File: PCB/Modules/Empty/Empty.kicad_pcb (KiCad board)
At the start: 2 copper layers, 29 x 59 mm, 4 parts, among them J1 In, J2 In, U1 SP720ABTG

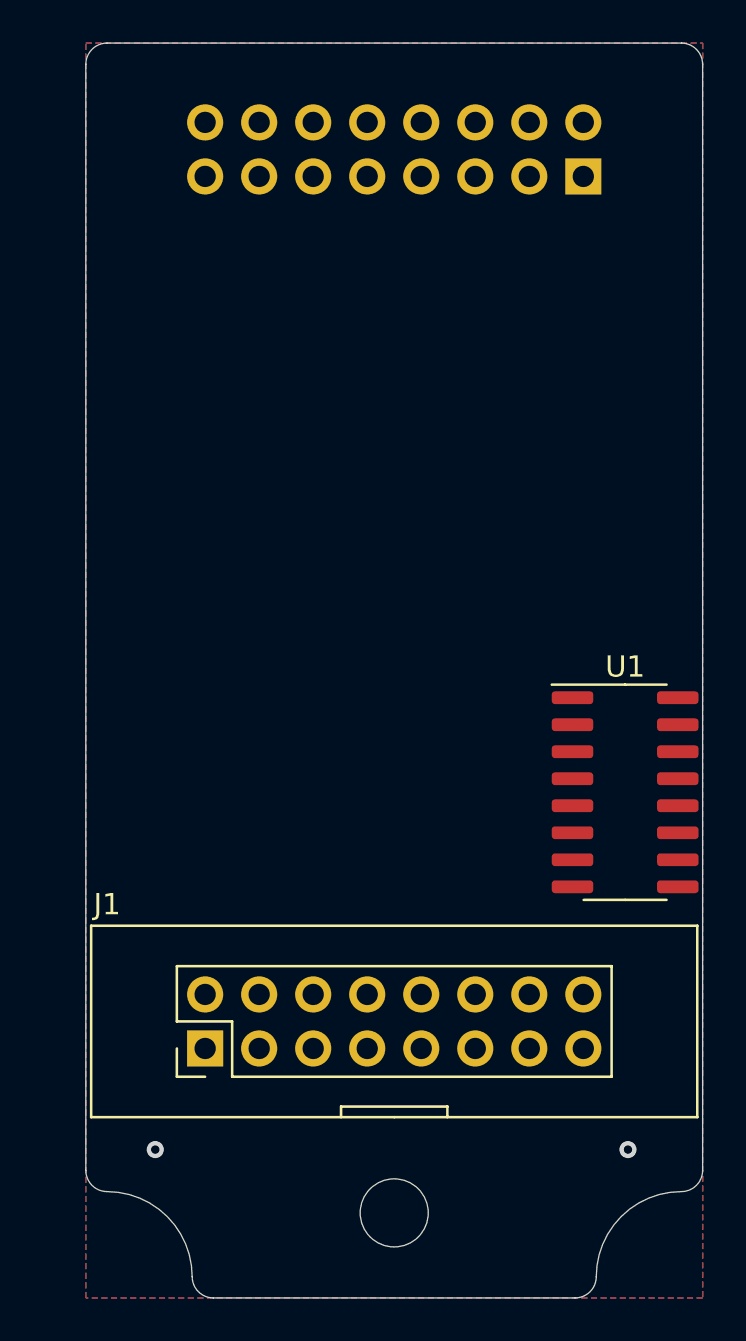
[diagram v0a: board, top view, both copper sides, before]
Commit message: Convert all KiCad to 6.0, clean up libraries, remove files that shouldn't be committed.
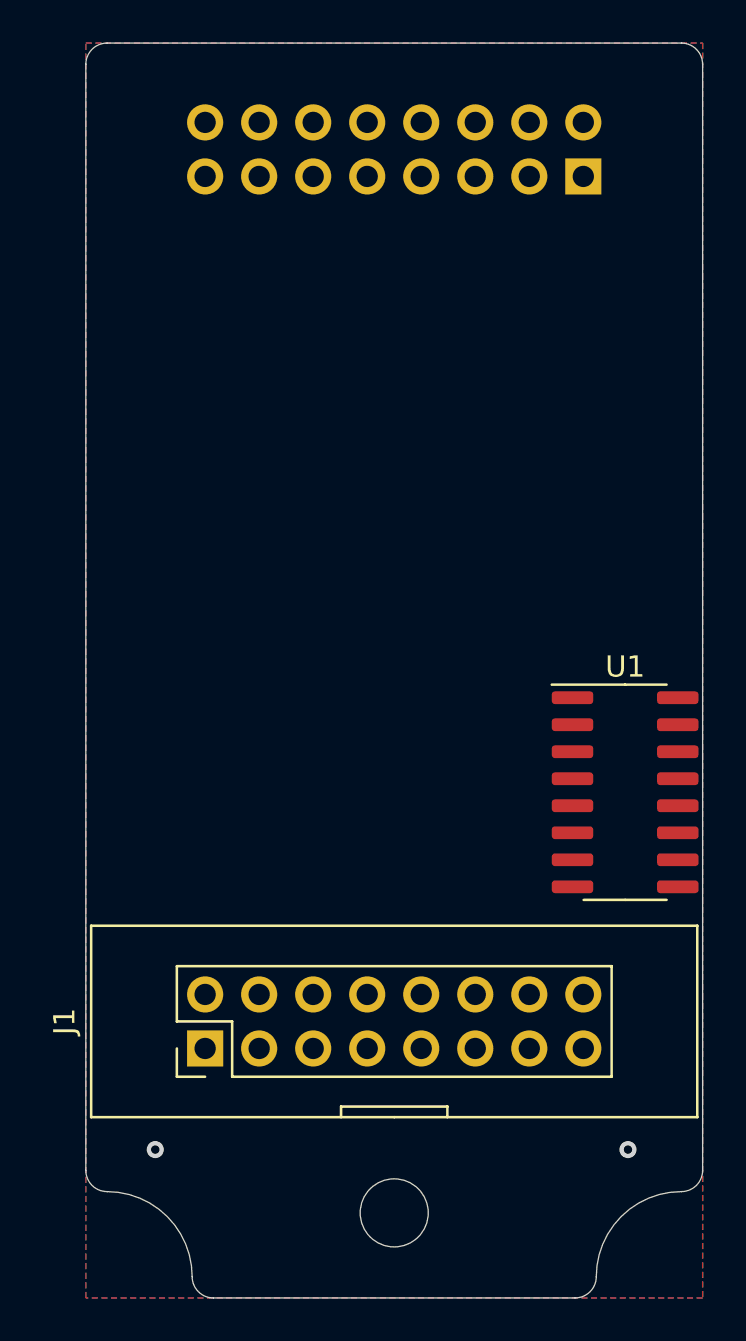
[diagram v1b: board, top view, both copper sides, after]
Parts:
- J1, J2: footprint Custom:PinHeader_2x08_P2.54mm_Vertical-Centered -> KTANE:PinHeader_2x08_P2.54mm_Vertical-Centered
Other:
- net class Default removed
- net class v Power removed
